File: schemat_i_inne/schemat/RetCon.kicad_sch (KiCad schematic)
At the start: 32 parts, among them J5 programming port, J6 USB_B_Micro, SW1 SW_SPDT, SW2 Home, SW3 triggerR, SW4 Select, SW5 triggerL, SW6 BumperL, SW7 BumperR, U1 ATmega1284P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

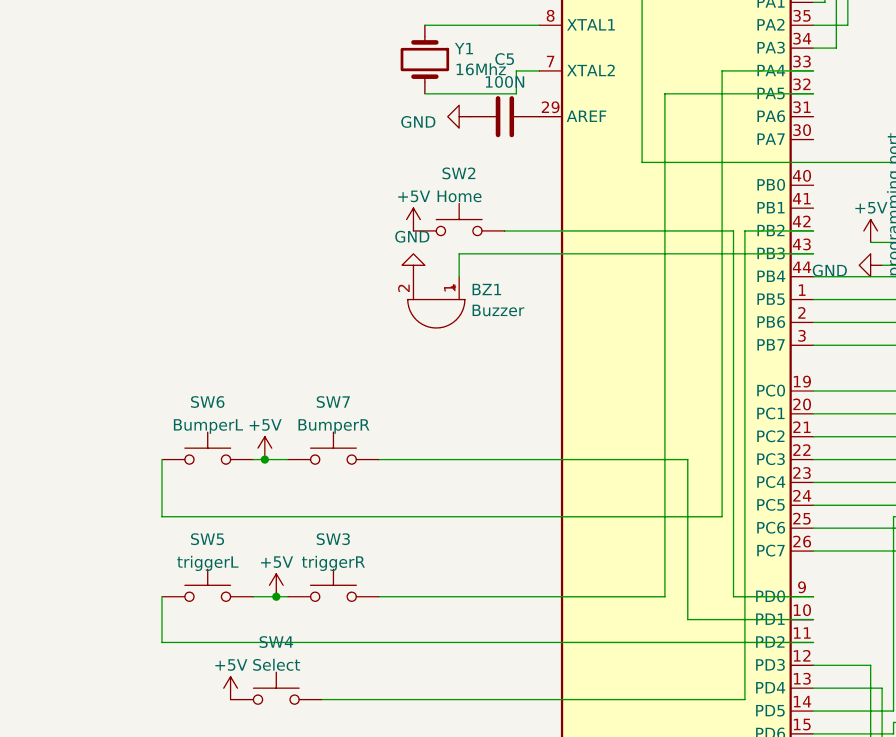
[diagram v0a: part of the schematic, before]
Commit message: RetCon config file and small updates
- names of triggers and bumpers updated
- schematic, board updated
- added picture how RetCon looks in reality
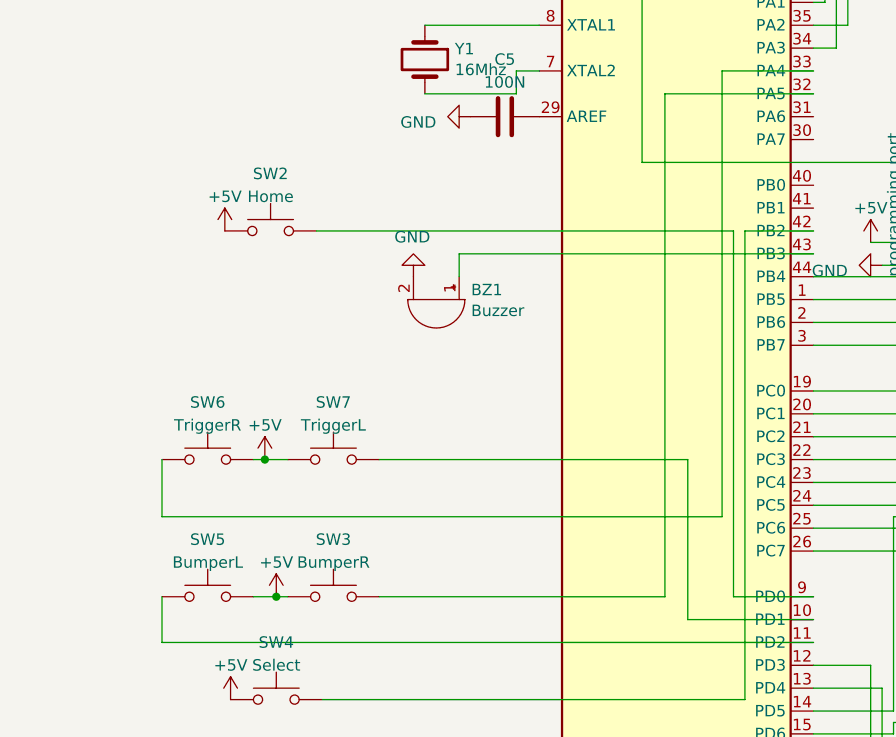
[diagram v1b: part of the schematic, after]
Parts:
- SW3: value triggerR -> BumperR
- SW5: value triggerL -> BumperL
- SW6: value BumperL -> TriggerR
- SW7: value BumperR -> TriggerL
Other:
- moved on the sheet: SW2
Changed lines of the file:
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@@
-    (stroke (width 0) (type default))
-  )
-  (wire (pts (xy 80.01 80.01) (xy 105.41 80.01))
     (stroke (width 0) (type default))
   )
@@
   )
   (wire (pts (xy 176.53 80.01) (xy 177.8 80.01))
+    (stroke (width 0) (type default))
+  )
+  (wire (pts (xy 59.055 80.01) (xy 105.41 80.01))
     (stroke (width 0) (type default))
   )
@@
       (effects (font (size 1.27 1.27)))
     )
-    (property "Value" "triggerR" (at 60.96 116.84 0)
+    (property "Value" "BumperR" (at 60.96 116.84 0)
       (effects (font (size 1.27 1.27)))
     )
@@
       (effects (font (size 1.27 1.27)))
     )
-    (property "Value" "triggerL" (at 46.99 116.84 0)
+    (property "Value" "BumperL" (at 46.99 116.84 0)
       (effects (font (size 1.27 1.27)))
     )
@@
       (effects (font (size 1.27 1.27)))
     )
-    (property "Value" "BumperR" (at 60.96 101.6 0)
+    (property "Value" "TriggerL" (at 60.96 101.6 0)
       (effects (font (size 1.27 1.27)))
     )
@@
     )
   )
-  (symbol (lib_id "Switch:SW_Push") (at 74.93 80.01 0) (unit 1)
-    (in_bom yes) (on_board yes) (dnp no) (fields_autoplaced)
-    (property "Reference" "SW2" (at 74.93 73.66 0)
-      (effects (font (size 1.27 1.27)))
-    )
-    (property "Value" "Home" (at 74.93 76.2 0)
-      (effects (font (size 1.27 1.27)))
-    )
-    (property "Footprint" "buttons:buttonSMD_withHoles" (at 74.93 74.93 0)
-      (effects (font (size 1.27 1.27)) hide)
-    )
-    (property "Datasheet" "~" (at 74.93 74.93 0)
+  (symbol (lib_id "Switch:SW_Push") (at 53.975 80.01 0) (unit 1)
+    (in_bom yes) (on_board yes) (dnp no) (fields_autoplaced)
+    (property "Reference" "SW2" (at 53.975 73.66 0)
+      (effects (font (size 1.27 1.27)))
+    )
+    (property "Value" "Home" (at 53.975 76.2 0)
+      (effects (font (size 1.27 1.27)))
+    )
+    (property "Footprint" "buttons:buttonSMD_withHoles" (at 53.975 74.93 0)
+      (effects (font (size 1.27 1.27)) hide)
+    )
+    (property "Datasheet" "~" (at 53.975 74.93 0)
       (effects (font (size 1.27 1.27)) hide)
     )
@@
     )
   )
-  (symbol (lib_name "+5V_8") (lib_id "power:+5V") (at 69.85 80.01 0) (unit 1)
-    (in_bom yes) (on_board yes) (dnp no) (fields_autoplaced)
-    (property "Reference" "#PWR029" (at 69.85 83.82 0)
-      (effects (font (size 1.27 1.27)) hide)
-    )
-    (property "Value" "+5V" (at 69.85 76.2 0)
-      (effects (font (size 1.27 1.27)))
-    )
-    (property "Footprint" "" (at 69.85 80.01 0)
-      (effects (font (size 1.27 1.27)) hide)
-    )
-    (property "Datasheet" "" (at 69.85 80.01 0)
+  (symbol (lib_name "+5V_8") (lib_id "power:+5V") (at 48.895 80.01 0) (unit 1)
+    (in_bom yes) (on_board yes) (dnp no) (fields_autoplaced)
+    (property "Reference" "#PWR029" (at 48.895 83.82 0)
+      (effects (font (size 1.27 1.27)) hide)
+    )
+    (property "Value" "+5V" (at 48.895 76.2 0)
+      (effects (font (size 1.27 1.27)))
+    )
+    (property "Footprint" "" (at 48.895 80.01 0)
+      (effects (font (size 1.27 1.27)) hide)
+    )
+    (property "Datasheet" "" (at 48.895 80.01 0)
       (effects (font (size 1.27 1.27)) hide)
     )
@@
       (effects (font (size 1.27 1.27)))
     )
-    (property "Value" "BumperL" (at 46.99 101.6 0)
-      (effects (font (size 1.27 1.27)))
-    )
+    (property "Value" "TriggerR" (at 46.99 101.6 0)
+      (effects (font (size 1.27 1.27)))
+    )
